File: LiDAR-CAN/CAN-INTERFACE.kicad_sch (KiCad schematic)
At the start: 19 parts, among them U3 TCAN4550RGY, Y2 40MHz

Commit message: Feature schematic revision 1
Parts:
- renumbered C22 to C26, C87 to C27, C23 to C28, C88 to C29, C24 to C30, C17 to C31, C18 to C32, C89 to C33, R13 to R27, R14 to R28, TP7 to TP23, TP13 to TP24, TP8 to TP25, TP9 to TP26, TP10 to TP27, TP11 to TP28, TP12 to TP29, U3 to U4
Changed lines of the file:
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@@
 		(dnp no)
 		(fields_autoplaced yes)
-		(property "Reference" "#PWR023"
+		(property "Reference" "#PWR054"
 			(at 127 82.55 0)
 			(effects
@@
 			(project "LiDAR-CAN"
 				(path "/56db6f21-0e4a-4321-bd8a-db37f1842dd9/acdb1e38-683e-41e3-b904-0eede9d7599d"
-					(reference "#PWR023")
+					(reference "#PWR054")
 					(unit 1)
 				)
@@
 		(dnp no)
 		(fields_autoplaced yes)
-		(property "Reference" "#PWR032"
+		(property "Reference" "#PWR058"
 			(at 44.45 135.89 0)
 			(effects
@@
 			(project "LiDAR-CAN"
 				(path "/56db6f21-0e4a-4321-bd8a-db37f1842dd9/acdb1e38-683e-41e3-b904-0eede9d7599d"
-					(reference "#PWR032")
+					(reference "#PWR058")
 					(unit 1)
 				)
@@
 		(on_board yes)
 		(dnp no)
-		(property "Reference" "C24"
+		(property "Reference" "C30"
 			(at 156.21 68.5799 0)
 			(effects
@@
 			(project "LiDAR-CAN"
 				(path "/56db6f21-0e4a-4321-bd8a-db37f1842dd9/acdb1e38-683e-41e3-b904-0eede9d7599d"
-					(reference "C24")
+					(reference "C30")
 					(unit 1)
 				)
@@
 		(dnp no)
 		(fields_autoplaced yes)
-		(property "Reference" "TP9"
+		(property "Reference" "TP26"
 			(at 231.14 146.5579 0)
 			(effects
@@
 			(project "LiDAR-CAN"
 				(path "/56db6f21-0e4a-4321-bd8a-db37f1842dd9/acdb1e38-683e-41e3-b904-0eede9d7599d"
-					(reference "TP9")
+					(reference "TP26")
 					(unit 1)
 				)
@@
 		(dnp no)
 		(fields_autoplaced yes)
-		(property "Reference" "#PWR025"
+		(property "Reference" "#PWR062"
 			(at 165.1 158.75 0)
 			(effects
@@
 			(project "LiDAR-CAN"
 				(path "/56db6f21-0e4a-4321-bd8a-db37f1842dd9/acdb1e38-683e-41e3-b904-0eede9d7599d"
-					(reference "#PWR025")
+					(reference "#PWR062")
 					(unit 1)
 				)
@@
 		(dnp no)
 		(fields_autoplaced yes)
-		(property "Reference" "U3"
+		(property "Reference" "U4"
 			(at 141.8433 137.16 0)
 			(effects
@@
 			(project ""
 				(path "/56db6f21-0e4a-4321-bd8a-db37f1842dd9/acdb1e38-683e-41e3-b904-0eede9d7599d"
-					(reference "U3")
+					(reference "U4")
 					(unit 1)
 				)
@@
 		(dnp no)
 		(fields_autoplaced yes)
-		(property "Reference" "#PWR024"
+		(property "Reference" "#PWR055"
 			(at 152.4 82.55 0)
 			(effects
@@
 			(project "LiDAR-CAN"
 				(path "/56db6f21-0e4a-4321-bd8a-db37f1842dd9/acdb1e38-683e-41e3-b904-0eede9d7599d"
-					(reference "#PWR024")
+					(reference "#PWR055")
 					(unit 1)
 				)
@@
 		(dnp no)
 		(fields_autoplaced yes)
-		(property "Reference" "#PWR026"
+		(property "Reference" "#PWR057"
 			(at 158.75 127 0)
 			(effects
@@
 			(project "LiDAR-CAN"
 				(path "/56db6f21-0e4a-4321-bd8a-db37f1842dd9/acdb1e38-683e-41e3-b904-0eede9d7599d"
-					(reference "#PWR026")
+					(reference "#PWR057")
 					(unit 1)
 				)
@@
 		(on_board yes)
 		(dnp no)
-		(property "Reference" "C18"
+		(property "Reference" "C32"
 			(at 50.8 120.904 90)
 			(effects
@@
 			(project "LiDAR-CAN"
 				(path "/56db6f21-0e4a-4321-bd8a-db37f1842dd9/acdb1e38-683e-41e3-b904-0eede9d7599d"
-					(reference "C18")
+					(reference "C32")
 					(unit 1)
 				)
@@
 		(on_board yes)
 		(dnp no)
-		(property "Reference" "C22"
+		(property "Reference" "C26"
 			(at 110.49 44.4499 0)
 			(effects
@@
 			(project "LiDAR-CAN"
 				(path "/56db6f21-0e4a-4321-bd8a-db37f1842dd9/acdb1e38-683e-41e3-b904-0eede9d7599d"
-					(reference "C22")
+					(reference "C26")
 					(unit 1)
 				)
@@
 		(on_board yes)
 		(dnp no)
-		(property "Reference" "C89"
+		(property "Reference" "C33"
 			(at 156.845 144.78 0)
 			(effects
@@
 			(project "LiDAR-CAN"
 				(path "/56db6f21-0e4a-4321-bd8a-db37f1842dd9/acdb1e38-683e-41e3-b904-0eede9d7599d"
-					(reference "C89")
+					(reference "C33")
 					(unit 1)
 				)
@@
 		(on_board yes)
 		(dnp no)
-		(property "Reference" "C87"
+		(property "Reference" "C27"
 			(at 118.745 44.45 0)
 			(effects
@@
 			(project "LiDAR-CAN"
 				(path "/56db6f21-0e4a-4321-bd8a-db37f1842dd9/acdb1e38-683e-41e3-b904-0eede9d7599d"
-					(reference "C87")
+					(reference "C27")
 					(unit 1)
 				)
@@
 		(dnp no)
 		(fields_autoplaced yes)
-		(property "Reference" "R14"
+		(property "Reference" "R28"
 			(at 110.49 100.3299 0)
 			(effects
@@
 			(project "LiDAR-CAN"
 				(path "/56db6f21-0e4a-4321-bd8a-db37f1842dd9/acdb1e38-683e-41e3-b904-0eede9d7599d"
-					(reference "R14")
+					(reference "R28")
 					(unit 1)
 				)
@@
 		(on_board yes)
 		(dnp no)
-		(property "Reference" "C17"
+		(property "Reference" "C31"
 			(at 50.8 108.204 90)
 			(effects
@@
 			(project "LiDAR-CAN"
 				(path "/56db6f21-0e4a-4321-bd8a-db37f1842dd9/acdb1e38-683e-41e3-b904-0eede9d7599d"
-					(reference "C17")
+					(reference "C31")
 					(unit 1)
 				)
@@
 		(dnp no)
 		(fields_autoplaced yes)
-		(property "Reference" "#PWR022"
+		(property "Reference" "#PWR061"
 			(at 139.7 146.05 0)
 			(effects
@@
 			(project "LiDAR-CAN"
 				(path "/56db6f21-0e4a-4321-bd8a-db37f1842dd9/acdb1e38-683e-41e3-b904-0eede9d7599d"
-					(reference "#PWR022")
+					(reference "#PWR061")
 					(unit 1)
 				)
@@
 		(dnp no)
 		(fields_autoplaced yes)
-		(property "Reference" "#PWR020"
+		(property "Reference" "#PWR052"
 			(at 127 58.42 0)
 			(effects
@@
 			(project "LiDAR-CAN"
 				(path "/56db6f21-0e4a-4321-bd8a-db37f1842dd9/acdb1e38-683e-41e3-b904-0eede9d7599d"
-					(reference "#PWR020")
+					(reference "#PWR052")
 					(unit 1)
 				)
@@
 		(dnp no)
 		(fields_autoplaced yes)
-		(property "Reference" "TP7"
+		(property "Reference" "TP23"
 			(at 193.04 146.5579 0)
 			(effects
@@
 			(project "LiDAR-CAN"
 				(path "/56db6f21-0e4a-4321-bd8a-db37f1842dd9/acdb1e38-683e-41e3-b904-0eede9d7599d"
-					(reference "TP7")
+					(reference "TP23")
 					(unit 1)
 				)
@@
 		(dnp no)
 		(fields_autoplaced yes)
-		(property "Reference" "#PWR031"
+		(property "Reference" "#PWR056"
 			(at 44.45 123.19 0)
 			(effects
@@
 			(project "LiDAR-CAN"
 				(path "/56db6f21-0e4a-4321-bd8a-db37f1842dd9/acdb1e38-683e-41e3-b904-0eede9d7599d"
-					(reference "#PWR031")
+					(reference "#PWR056")
 					(unit 1)
 				)
@@
 		(dnp no)
 		(fields_autoplaced yes)
-		(property "Reference" "#PWR019"
+		(property "Reference" "#PWR051"
 			(at 114.3 58.42 0)
 			(effects
@@
 			(project "LiDAR-CAN"
 				(path "/56db6f21-0e4a-4321-bd8a-db37f1842dd9/acdb1e38-683e-41e3-b904-0eede9d7599d"
-					(reference "#PWR019")
+					(reference "#PWR051")
 					(unit 1)
 				)
@@
 		(dnp no)
 		(fields_autoplaced yes)
-		(property "Reference" "TP10"
+		(property "Reference" "TP27"
 			(at 243.84 146.5579 0)
 			(effects
@@
 			(project "LiDAR-CAN"
 				(path "/56db6f21-0e4a-4321-bd8a-db37f1842dd9/acdb1e38-683e-41e3-b904-0eede9d7599d"
-					(reference "TP10")
+					(reference "TP27")
 					(unit 1)
 				)
@@
 		(dnp no)
 		(fields_autoplaced yes)
-		(property "Reference" "R13"
+		(property "Reference" "R27"
 			(at 97.79 100.3299 0)
 			(effects
@@
 			(project "LiDAR-CAN"
 				(path "/56db6f21-0e4a-4321-bd8a-db37f1842dd9/acdb1e38-683e-41e3-b904-0eede9d7599d"
-					(reference "R13")
+					(reference "R27")
 					(unit 1)
 				)
@@
 		(dnp no)
 		(fields_autoplaced yes)
-		(property "Reference" "TP11"
+		(property "Reference" "TP28"
 			(at 256.54 146.5579 0)
 			(effects
@@
 			(project "LiDAR-CAN"
 				(path "/56db6f21-0e4a-4321-bd8a-db37f1842dd9/acdb1e38-683e-41e3-b904-0eede9d7599d"
-					(reference "TP11")
+					(reference "TP28")
 					(unit 1)
 				)
@@
 		(dnp no)
 		(fields_autoplaced yes)
-		(property "Reference" "TP12"
+		(property "Reference" "TP29"
 			(at 269.24 146.5579 0)
 			(effects
@@
 			(project "LiDAR-CAN"
 				(path "/56db6f21-0e4a-4321-bd8a-db37f1842dd9/acdb1e38-683e-41e3-b904-0eede9d7599d"
-					(reference "TP12")
+					(reference "TP29")
 					(unit 1)
 				)
@@
 		(on_board yes)
 		(dnp no)
-		(property "Reference" "C23"
+		(property "Reference" "C28"
 			(at 110.49 68.5799 0)
 			(effects
@@
 			(project "LiDAR-CAN"
 				(path "/56db6f21-0e4a-4321-bd8a-db37f1842dd9/acdb1e38-683e-41e3-b904-0eede9d7599d"
-					(reference "C23")
+					(reference "C28")
 					(unit 1)
 				)
@@
 		(dnp no)
 		(fields_autoplaced yes)
-		(property "Reference" "TP13"
+		(property "Reference" "TP24"
 			(at 205.74 146.5579 0)
 			(effects
@@
 			(project "LiDAR-CAN"
 				(path "/56db6f21-0e4a-4321-bd8a-db37f1842dd9/acdb1e38-683e-41e3-b904-0eede9d7599d"
-					(reference "TP13")
+					(reference "TP24")
 					(unit 1)
 				)
@@
 		(dnp no)
 		(fields_autoplaced yes)
-		(property "Reference" "#PWR021"
+		(property "Reference" "#PWR053"
 			(at 114.3 82.55 0)
 			(effects
@@
 			(project "LiDAR-CAN"
 				(path "/56db6f21-0e4a-4321-bd8a-db37f1842dd9/acdb1e38-683e-41e3-b904-0eede9d7599d"
-					(reference "#PWR021")
+					(reference "#PWR053")
 					(unit 1)
 				)
@@
 		(on_board yes)
 		(dnp no)
-		(property "Reference" "C88"
+		(property "Reference" "C29"
 			(at 118.745 68.58 0)
 			(effects
@@
 			(project "LiDAR-CAN"
 				(path "/56db6f21-0e4a-4321-bd8a-db37f1842dd9/acdb1e38-683e-41e3-b904-0eede9d7599d"
-					(reference "C88")
+					(reference "C29")
 					(unit 1)
 				)
@@
 		(dnp no)
 		(fields_autoplaced yes)
-		(property "Reference" "#PWR034"
+		(property "Reference" "#PWR060"
 			(at 67.31 135.89 0)
 			(effects
@@
 			(project "LiDAR-CAN"
 				(path "/56db6f21-0e4a-4321-bd8a-db37f1842dd9/acdb1e38-683e-41e3-b904-0eede9d7599d"
-					(reference "#PWR034")
+					(reference "#PWR060")
 					(unit 1)
 				)
@@
 		(dnp no)
 		(fields_autoplaced yes)
-		(property "Reference" "#PWR033"
+		(property "Reference" "#PWR059"
 			(at 59.69 135.89 0)
 			(effects
@@
 			(project "LiDAR-CAN"
 				(path "/56db6f21-0e4a-4321-bd8a-db37f1842dd9/acdb1e38-683e-41e3-b904-0eede9d7599d"
-					(reference "#PWR033")
+					(reference "#PWR059")
 					(unit 1)
 				)
@@
 		(dnp no)
 		(fields_autoplaced yes)
-		(property "Reference" "TP8"
+		(property "Reference" "TP25"
 			(at 218.44 146.5579 0)
 			(effects
@@
 			(project "LiDAR-CAN"
 				(path "/56db6f21-0e4a-4321-bd8a-db37f1842dd9/acdb1e38-683e-41e3-b904-0eede9d7599d"
-					(reference "TP8")
-					(unit 1)
-				)
+					(reference "TP25")
+					(unit 1)
+				)

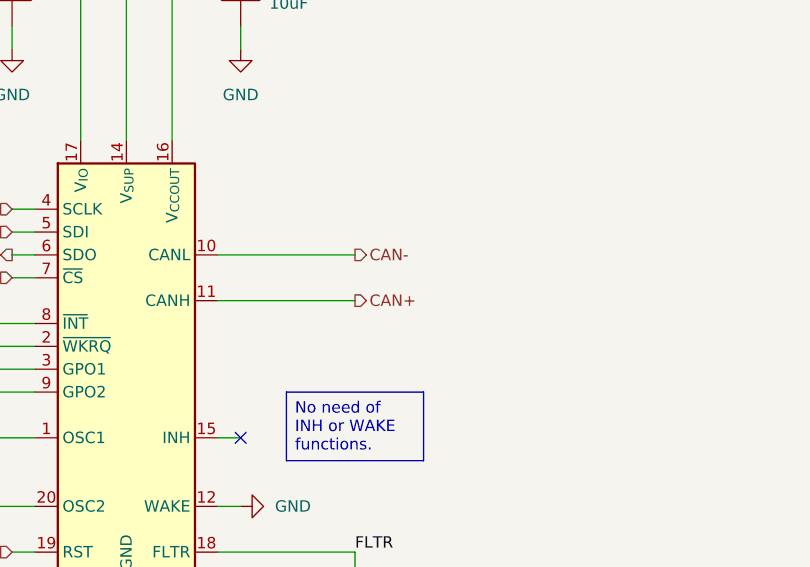
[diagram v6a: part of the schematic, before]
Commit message: Setup PCB stackup and routing
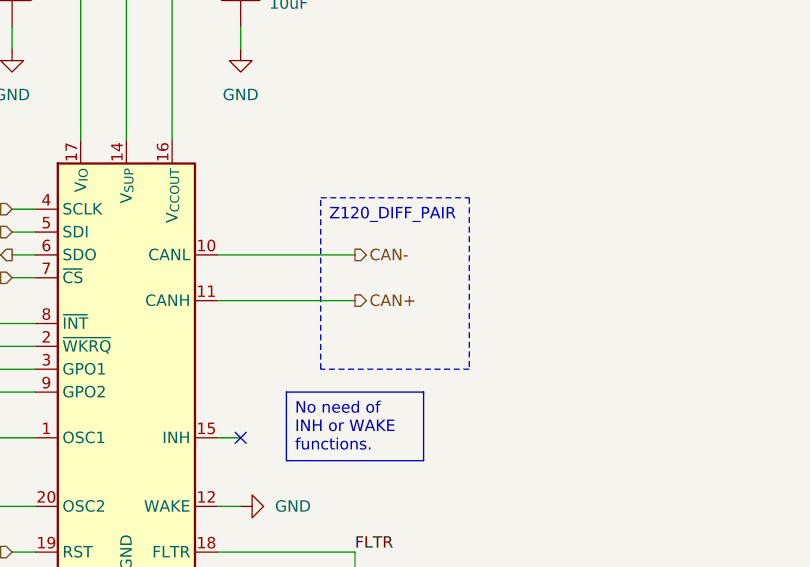
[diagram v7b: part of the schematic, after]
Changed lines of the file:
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@@
+		)
+	)
+	(text_box "Z120_DIFF_PAIR"
+		(exclude_from_sim no)
+		(at 161.29 92.71 0)
+		(size 16.51 19.05)
+		(margins 0.9525 0.9525 0.9525 0.9525)
+		(stroke
+			(width 0)
+			(type dash)
+		)
+		(fill
+			(type none)
+		)
+		(effects
+			(font
+				(size 1.27 1.27)
+			)
+			(justify left top)
 		)
 	)

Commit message: Start placement of components
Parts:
- TP23, TP24, TP25, TP26, TP27, TP28, TP29: footprint TestPoint:TestPoint_Pad_D1.5mm -> TestPoint:TestPoint_Pad_D1.0mm
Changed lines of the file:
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@@
 		(exclude_from_sim no)
 		(in_bom no)
-		(on_board no)
+		(on_board yes)
 		(dnp no)
 		(fields_autoplaced yes)
@@
 			)
 		)
-		(property "Footprint" "TestPoint:TestPoint_Pad_D1.5mm"
+		(property "Footprint" "TestPoint:TestPoint_Pad_D1.0mm"
 			(at 233.68 151.13 0)
 			(effects
@@
 		(exclude_from_sim no)
 		(in_bom no)
-		(on_board no)
+		(on_board yes)
 		(dnp no)
 		(fields_autoplaced yes)
@@
 			)
 		)
-		(property "Footprint" "TestPoint:TestPoint_Pad_D1.5mm"
+		(property "Footprint" "TestPoint:TestPoint_Pad_D1.0mm"
 			(at 195.58 151.13 0)
 			(effects
@@
 		(exclude_from_sim no)
 		(in_bom no)
-		(on_board no)
+		(on_board yes)
 		(dnp no)
 		(fields_autoplaced yes)
@@
 			)
 		)
-		(property "Footprint" "TestPoint:TestPoint_Pad_D1.5mm"
+		(property "Footprint" "TestPoint:TestPoint_Pad_D1.0mm"
 			(at 246.38 151.13 0)
 			(effects
@@
 		(exclude_from_sim no)
 		(in_bom no)
-		(on_board no)
+		(on_board yes)
 		(dnp no)
 		(fields_autoplaced yes)
@@
 			)
 		)
-		(property "Footprint" "TestPoint:TestPoint_Pad_D1.5mm"
+		(property "Footprint" "TestPoint:TestPoint_Pad_D1.0mm"
 			(at 259.08 151.13 0)
 			(effects
@@
 		(exclude_from_sim no)
 		(in_bom no)
-		(on_board no)
+		(on_board yes)
 		(dnp no)
 		(fields_autoplaced yes)
@@
 			)
 		)
-		(property "Footprint" "TestPoint:TestPoint_Pad_D1.5mm"
+		(property "Footprint" "TestPoint:TestPoint_Pad_D1.0mm"
 			(at 271.78 151.13 0)
 			(effects
@@
 		(exclude_from_sim no)
 		(in_bom no)
-		(on_board no)
+		(on_board yes)
 		(dnp no)
 		(fields_autoplaced yes)
@@
 			)
 		)
-		(property "Footprint" "TestPoint:TestPoint_Pad_D1.5mm"
+		(property "Footprint" "TestPoint:TestPoint_Pad_D1.0mm"
 			(at 208.28 151.13 0)
 			(effects
@@
 		(exclude_from_sim no)
 		(in_bom no)
-		(on_board no)
+		(on_board yes)
 		(dnp no)
 		(fields_autoplaced yes)
@@
 			)
 		)
-		(property "Footprint" "TestPoint:TestPoint_Pad_D1.5mm"
+		(property "Footprint" "TestPoint:TestPoint_Pad_D1.0mm"
 			(at 220.98 151.13 0)
 			(effects
